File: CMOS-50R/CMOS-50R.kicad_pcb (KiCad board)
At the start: 4 copper layers, 52.1 x 20.3 mm, 56 parts, among them J1 Conn_01x06_Male, J11 Conn_Coaxial, J2 Conn_01x02_Male, J21 Conn_Coaxial, J3 Conn_Coaxial, J31 Conn_Coaxial, J41 Conn_Coaxial, U1 7404, U2 7404, U3 7404, U4 7404

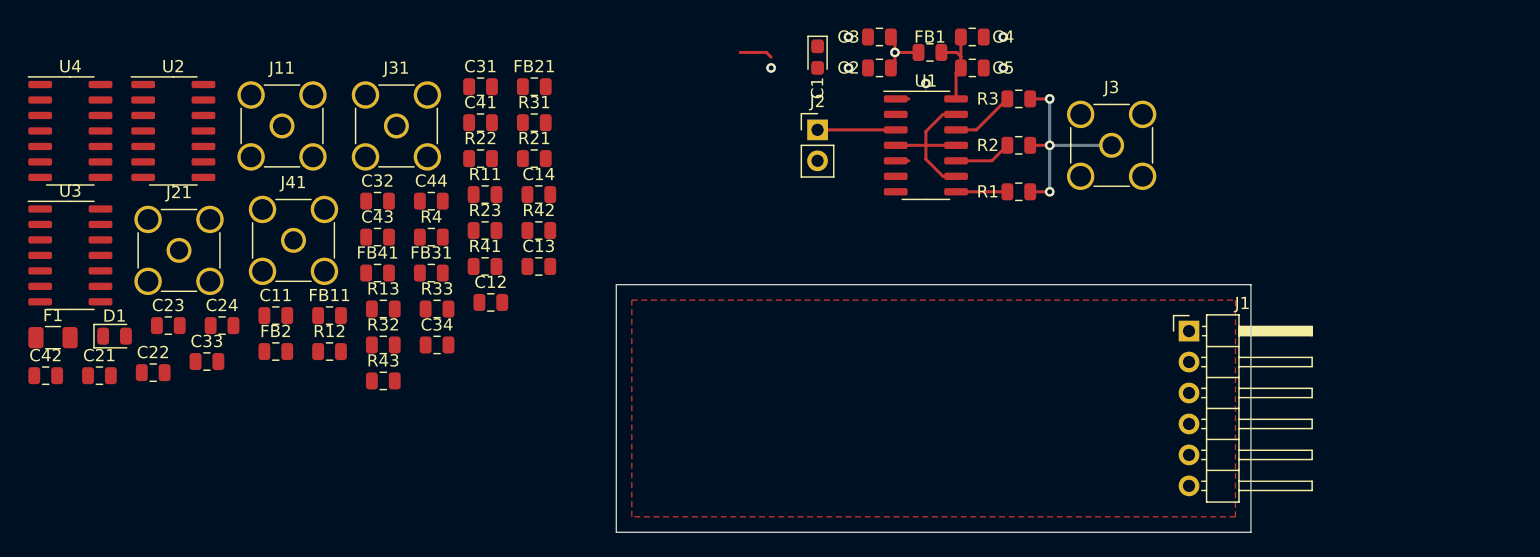
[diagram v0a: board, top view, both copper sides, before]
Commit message: updated polarity protect and filter caps, layout progress
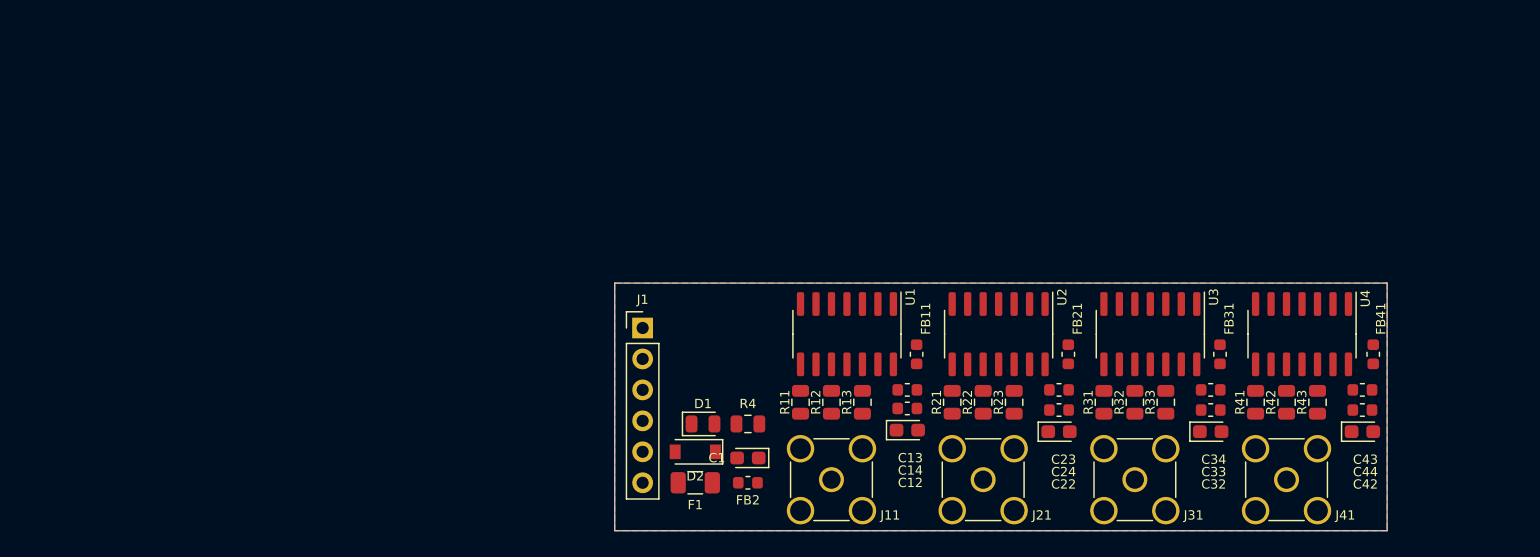
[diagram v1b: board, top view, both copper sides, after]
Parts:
- removed C11, C2, C21, C31, C4, C41: 0.1u, Capacitor_SMD:C_0805_2012Metric
- removed C3, C5: 1n, Capacitor_SMD:C_0805_2012Metric
- removed FB1: Ferrite_Bead_Small, Inductor_SMD:L_0805_2012Metric
- removed J2: Conn_01x02_Male, Connector_PinHeader_2.54mm:PinHeader_1x02_P2.54mm_Vertical
- removed J3: Conn_Coaxial, Connector_Coaxial:SMA_Amphenol_132134-11_Vertical
- removed R1, R2, R3: 150, Resistor_SMD:R_0805_2012Metric
- added D2: 5817/5819, Diode_SMD:D_SOD-123, F.Cu at (81.4, 72.1)
- C12, C22, C32, C42: value 1n -> 10u; footprint Capacitor_SMD:C_0805_2012Metric -> Capacitor_Tantalum_SMD:CP_EIA-2012-12_Kemet-R
- C13, C14, C23, C24, C33, C34, C43, C44: footprint Capacitor_SMD:C_0805_2012Metric -> Capacitor_SMD:C_0603_1608Metric
- FB11, FB2, FB21, FB31, FB41: footprint Inductor_SMD:L_0805_2012Metric -> Inductor_SMD:L_0603_1608Metric
- J1: footprint Connector_PinHeader_2.54mm:PinHeader_1x06_P2.54mm_Horizontal -> Connector_PinHeader_2.54mm:PinHeader_1x06_P2.54mm_Vertical
- moved C42 108.1 mm to (136.1, 70.5)
- moved U4 102.4 mm to (131.2, 62.5), turned to 270 degrees
- moved U3 88.9 mm to (118.7, 62.5), turned to 270 degrees
- moved J41 83.8 mm to (129.9, 74.4), turned to 270 degrees
- moved C33 82.5 mm to (123.7, 68.7)
- moved FB41 82.0 mm to (137.0, 64.1), turned to 90 degrees
- moved C43 81.8 mm to (136.1, 67.1)
- moved C44 78.3 mm to (136.1, 68.7)
- moved R43 76.7 mm to (132.5, 68.1), turned to 90 degrees
- moved C22 74.5 mm to (111.3, 70.5)
- moved C23 73.4 mm to (111.3, 68.7)
- moved C32 70.9 mm to (123.7, 70.5)
- moved U2 69.7 mm to (106.3, 62.5), turned to 270 degrees
- moved C24 68.9 mm to (111.3, 67.1)
- moved J21 68.6 mm to (105.0, 74.4), turned to 270 degrees
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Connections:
- C12 pad 1: VDD -> Vcc
- C22 pad 1: VDD -> Vcc
- C32 pad 1: VDD -> Vcc
- C42 pad 1: VDD -> Vcc
- F1 pad 2: Net-(F1-Pad2) -> /VDD_IN
- J1 pad 5: Net-(F1-Pad2) -> GND
- J1 pad 6: GND -> /VDD_IN
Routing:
- net Net-(J3-Pad1): track 17.5 -> 0.00 mm, vias 3 -> 0
- net Net-(U1-Pad11): track 13.3 -> 0.00 mm
- net Vcc: track 7.55 -> 0.00 mm
- net Net-(J2-Pad1): track 6.42 -> 0.00 mm
- net Net-(R3-Pad2): track 5.26 -> 0.00 mm
- net VDD: track 4.75 -> 0.00 mm, vias 1 -> 0
- net Net-(R2-Pad2): track 4.73 -> 0.00 mm
- net Net-(R1-Pad2): track 4.21 -> 0.00 mm
- net /crtl1: track 2.70 -> 0.00 mm
- net GND: track 2.22 -> 0.00 mm
- net (no net): vias 6 -> 0
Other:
- board size 52.1 x 20.3 mm -> 63.4 x 20.3 mm

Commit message: layout updates
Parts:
- moved FB2 6.86 mm to (85.7, 67.8)
- moved C1 6.61 mm to (85.6, 66.0)
- moved D1 4.88 mm to (82.8, 74.7)
- moved R4 4.87 mm to (86.4, 74.7)
- moved D2 4.12 mm to (84.8, 69.8)
- moved F1 4.12 mm to (84.8, 72.4)
- moved C44 3.94 mm to (137.5, 65.0)
- moved C14 3.82 mm to (100.2, 65.0)
- moved J1 2.82 mm to (78.7, 59.7)
- moved J41 2.79 mm to (131.3, 72.0)
- moved J11 2.79 mm to (94.0, 72.0)
- moved J21 2.79 mm to (106.4, 72.0)
- moved J31 2.79 mm to (118.9, 72.0)
- moved R42 2.47 mm to (131.3, 66.0)
- moved FB11 2.47 mm to (101.0, 62.1)
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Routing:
- removed copper zone on GND.Cu, net GND
- removed copper zone on PWR.Cu, net VDD
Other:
- copper layers 4 -> 2

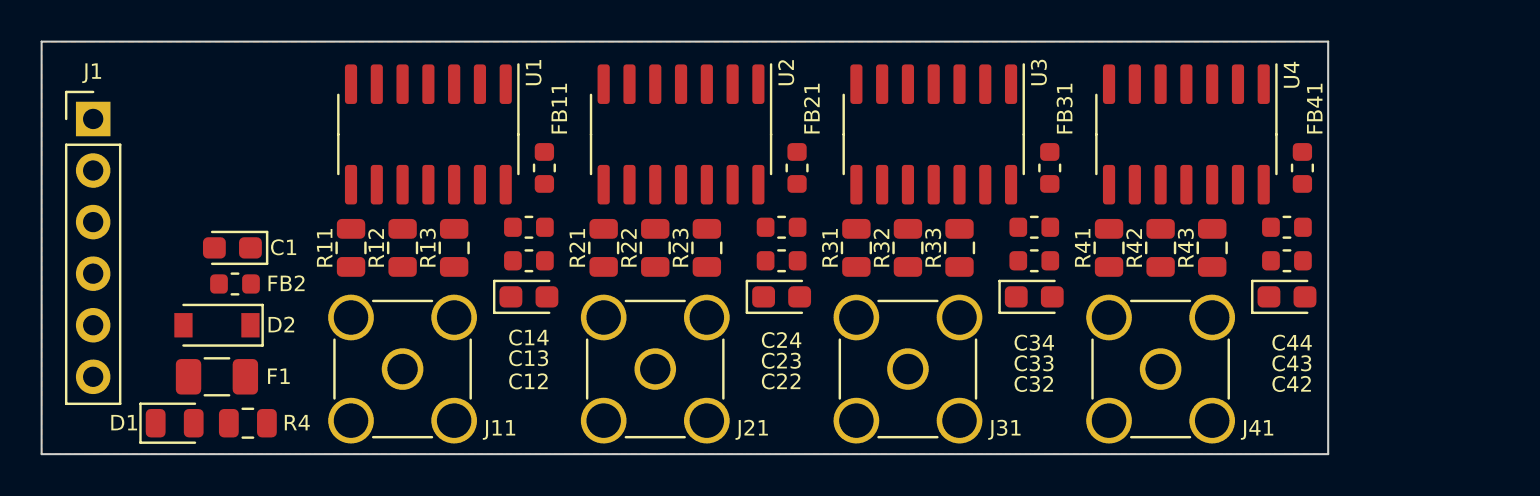
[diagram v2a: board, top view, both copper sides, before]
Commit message: Added fiducials and mounting hole
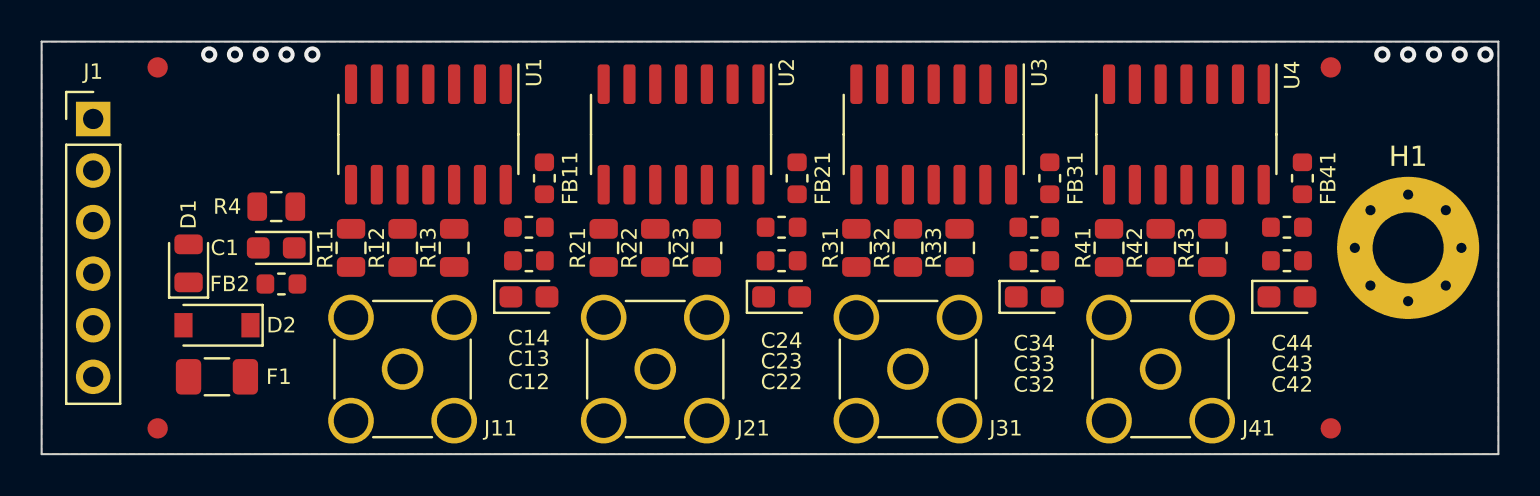
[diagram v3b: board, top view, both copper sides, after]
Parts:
- added FID1: Fiducial, Fiducial:Fiducial_1mm_Mask2mm, F.Cu at (81.9, 57.1)
- added FID2: Fiducial, Fiducial:Fiducial_1mm_Mask2mm, F.Cu at (81.9, 74.9)
- added FID3: Fiducial, Fiducial:Fiducial_1mm_Mask2mm, F.Cu at (139.7, 57.1)
- added FID4: Fiducial, Fiducial:Fiducial_1mm_Mask2mm, F.Cu at (139.7, 74.9)
- added H1: MountingHole_Pad, MountingHole:MountingHole_3.5mm_Pad_Via, F.Cu at (143.5, 66.0)
- moved R4 10.8 mm to (87.8, 64.0)
- moved D1 7.90 mm to (83.4, 66.8), turned to 90 degrees
- moved FB2 2.29 mm to (88.0, 67.8)
- moved C1 2.16 mm to (87.8, 66.0)
- moved FB11 0.51 mm to (101.0, 62.6)
- moved FB21 0.51 mm to (113.4, 62.6)
- moved FB31 0.51 mm to (125.9, 62.6)
- moved FB41 0.51 mm to (138.3, 62.6)
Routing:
- net GND: vias 0 -> 10
- added copper zone on B.Cu, net GND
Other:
- board size 63.4 x 20.3 mm -> 71.8 x 20.3 mm

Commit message: First full functional layout trace route
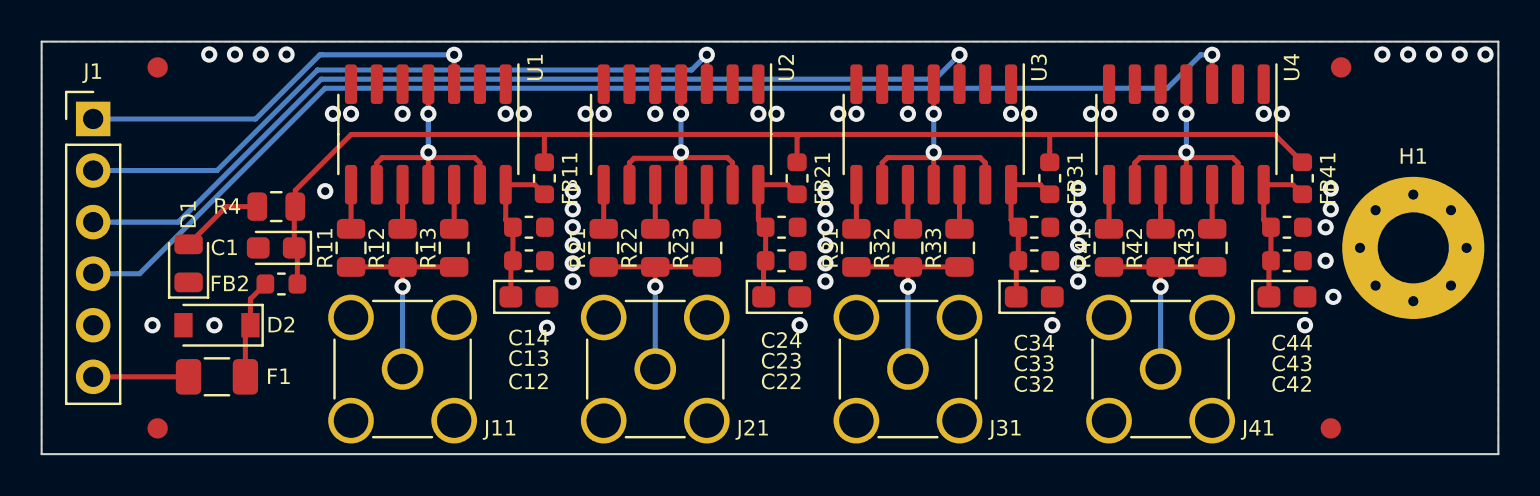
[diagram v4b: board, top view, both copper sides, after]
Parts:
- U1, U2, U3, U4: value 7404 -> 74AHC04
- moved FID3 0.51 mm to (140.2, 57.1)
- moved H1 0.25 mm to (143.8, 66.0)
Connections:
- C12 pad 1: Vcc -> Net-(C12-Pad1)
- C13 pad 1: Vcc -> Net-(C12-Pad1)
- C14 pad 1: Vcc -> Net-(C12-Pad1)
- C22 pad 1: Vcc -> Net-(C22-Pad1)
- C23 pad 1: Vcc -> Net-(C22-Pad1)
- C24 pad 1: Vcc -> Net-(C22-Pad1)
- C32 pad 1: Vcc -> Net-(C32-Pad1)
- C33 pad 1: Vcc -> Net-(C32-Pad1)
- C34 pad 1: Vcc -> Net-(C32-Pad1)
- C42 pad 1: Vcc -> Net-(C42-Pad1)
- C43 pad 1: Vcc -> Net-(C42-Pad1)
- C44 pad 1: Vcc -> Net-(C42-Pad1)
- FB11 pad 1: Vcc -> Net-(C12-Pad1)
- FB21 pad 1: Vcc -> Net-(C22-Pad1)
- FB31 pad 1: Vcc -> Net-(C32-Pad1)
- FB41 pad 1: Vcc -> Net-(C42-Pad1)
- J1 pad 1: /crtl1 -> /ctrl1
- U1 pad 14: Vcc -> Net-(C12-Pad1)
- U2 pad 14: Vcc -> Net-(C22-Pad1)
- U3 pad 14: Vcc -> Net-(C32-Pad1)
- U4 pad 14: Vcc -> Net-(C42-Pad1)
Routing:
- net /ctrl4: track 0.00 -> 61.0 mm, vias 0 -> 1
- net VDD: track 0.00 -> 60.2 mm
- net /ctrl3: track 0.00 -> 47.5 mm, vias 0 -> 1
- net /ctrl2: track 0.00 -> 34.0 mm, vias 0 -> 1
- net /ctrl1: track 0.00 -> 20.7 mm, vias 0 -> 1
- net Net-(U1-Pad11): track 0.00 -> 13.9 mm, vias 0 -> 2
- net Net-(U3-Pad11): track 0.00 -> 12.5 mm, vias 0 -> 2
- net Net-(U2-Pad11): track 0.00 -> 12.5 mm, vias 0 -> 2
- net Net-(U4-Pad11): track 0.00 -> 12.5 mm, vias 0 -> 2
- net Net-(J41-Pad1): track 0.00 -> 10.1 mm, vias 0 -> 1
- net Net-(J31-Pad1): track 0.00 -> 10.1 mm, vias 0 -> 1
- net Net-(J21-Pad1): track 0.00 -> 10.1 mm, vias 0 -> 1
- net Net-(J11-Pad1): track 0.00 -> 10.1 mm, vias 0 -> 1
- net Net-(C32-Pad1): track 0.00 -> 7.81 mm
- net Net-(C22-Pad1): track 0.00 -> 7.81 mm
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
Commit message: finished annotations
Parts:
- J1: value Conn_01x06_Male -> PMOD
- J11, J21, J31, J41: value Conn_Coaxial -> SMA
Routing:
- net GND: vias 59 -> 61
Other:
- board text added: "0V"
- board text added: "27/08/2019"
- board text added: "3.3v"
- board text added: "5v"
- board text added: "I1"
- board text added: "I2"
- board text added: "I3"
- board text added: "I4"
- board text added: "SN:"
- board text added: "github.com/cpgmoore /emods/CMOS-50R"
